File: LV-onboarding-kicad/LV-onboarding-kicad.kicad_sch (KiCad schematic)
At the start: 0 parts

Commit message: 2nd commit
changed the text in the bottom left of schematic
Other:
- title: ${BSPD_Circuit} -> BSPD_Circuit
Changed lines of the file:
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@@
 	(paper "A")
 	(title_block
-		(title "${BSPD_Circuit}")
+		(title "BSPD_Circuit")
 		(date "${CURRENT_DATE}")
 		(rev "${REVISION}")
 		(company "Formula Slug")
 		(comment 1 "Charles Ge")
-		(comment 3 "${COMMENT2}")
+		(comment 2 "Figured out how to push onto github after 4 hrs. I think in the future")
+		(comment 3 "it would be easier to hold github workshops with the desktop app")
+		(comment 4 "unless there is a benefit I am not aware of that is only in terminal.")
 	)
 	(sheet_instances

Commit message: commit1 friday
just put the haas sensor symbol on schematic
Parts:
- added U1: Current Transducer HASS 50 ... 600-S, Package_DFN_QFN:QFN-20-1EP_5x5mm_P0.65mm_EP3.35x3.35mm, symbol Connector:Conn_01x04_Pin
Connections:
- new net +5V: U1.4 (Pin_4)
- new net GND: U1.3 (Pin_3)
- new net OUTPUT: U1.2 (Pin_2)
- new net Vref: U1.1 (Pin_1)
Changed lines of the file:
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@@
 		(comment 4 "unless there is a benefit I am not aware of that is only in terminal.")
+	)
+	(label "GND"
+		(at 93.98 93.98 0)
+		(effects
+			(font
+				(size 1.27 1.27)
+			)
+			(justify left bottom)
+		)
+	)
+	(label "Vref"
+		(at 93.98 88.9 0)
+		(effects
+			(font
+				(size 1.27 1.27)
+			)
+			(justify left bottom)
+		)
+	)
+	(label "OUTPUT"
+		(at 93.98 91.44 0)
+		(effects
+			(font
+				(size 1.27 1.27)
+			)
+			(justify left bottom)
+		)
+	)
+	(label "+5V"
+		(at 93.98 96.52 0)
+		(effects
+			(font
+				(size 1.27 1.27)
+			)
+			(justify left bottom)
+		)
+	)
+	(symbol
+		(lib_id "Connector:Conn_01x04_Pin")
+		(at 88.9 91.44 0)
+		(unit 1)
+		(body_style 1)
+		(exclude_from_sim no)
+		(in_bom yes)
+		(on_board yes)
+		(in_pos_files yes)
+		(dnp no)
+		(fields_autoplaced yes)
+		(property "Reference" "U1"
+			(at 89.535 83.82 0)
+			(show_name no)
+			(do_not_autoplace no)
+			(effects
+				(font
+					(size 1.27 1.27)
+				)
+			)
+		)
+		(property "Value" "Current Transducer HASS 50 ... 600-S"
+			(at 89.535 86.36 0)
+			(show_name no)
+			(do_not_autoplace no)
+			(effects
+				(font
+					(size 1.27 1.27)
+				)
+			)
+		)
+		(property "Footprint" "Package_DFN_QFN:QFN-20-1EP_5x5mm_P0.65mm_EP3.35x3.35mm"
+			(at 88.9 91.44 0)
+			(hide yes)
+			(show_name no)
+			(do_not_autoplace no)
+			(effects
+				(font
+					(size 1.27 1.27)
+				)
+			)
+		)
+		(property "Datasheet" ""
+			(at 88.9 91.44 0)
+			(hide yes)
+			(show_name no)
+			(do_not_autoplace no)
+			(effects
+				(font
+					(size 1.27 1.27)
+				)
+			)
+		)
+		(property "Description" "Generic connector, single row, 01x04, script generated"
+			(at 88.9 91.44 0)
+			(hide yes)
+			(show_name no)
+			(do_not_autoplace no)
+			(effects
+				(font
+					(size 1.27 1.27)
+				)
+			)
+		)
+		(pin "3"
+		)
+		(pin "1"
+		)
+		(pin "4"
+		)
+		(pin "2"
+		)
+		(instances
+			(project "LV-onboarding-kicad"
+				(path "/e994741c-7c7d-4124-9d00-43b883baa61d"
+					(reference "U1")
+					(unit 1)
+				)
+			)
+		)
 	)
 	(sheet_instances

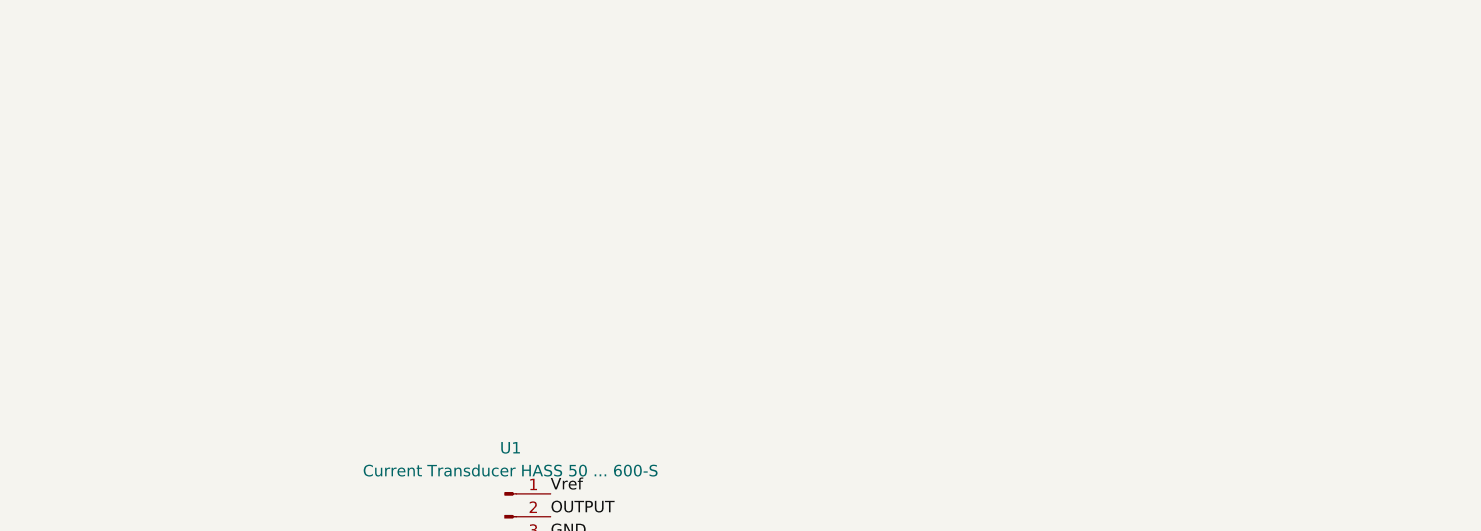
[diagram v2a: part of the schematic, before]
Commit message: kicad changes
put a couple more symbols into kicad schematic for BSPD
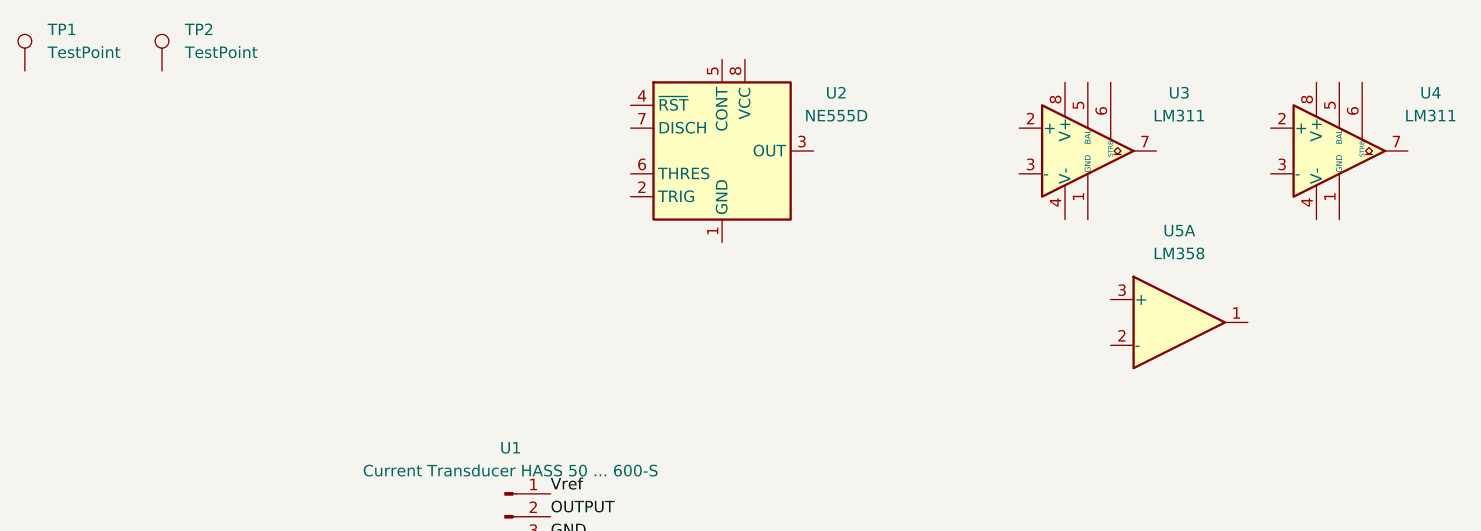
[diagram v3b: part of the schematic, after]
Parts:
- added TP1: TestPoint, Relay_THT:Relay_DPDT_Schrack-RT2-FormC_RM5mm, symbol Connector:TestPoint
- added TP2: TestPoint, symbol Connector:TestPoint
- added U2: NE555D, Package_SO:SOIC-8_3.9x4.9mm_P1.27mm, symbol Timer:NE555D
- added U3: LM311, Package_DIP:DIP-14_W7.62mm, symbol Comparator:LM311
- added U4: LM311, symbol Comparator:LM311
- added U5: LM358, Package_DFN_QFN:DFN-8-1EP_2x2mm_P0.5mm_EP1.05x1.75mm, symbol Amplifier_Operational:LM358

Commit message: ?
why it want me to commit again
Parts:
- removed U3: LM311, Package_DIP:DIP-14_W7.62mm, symbol Comparator:LM311
- removed U4: LM311, symbol Comparator:LM311
- removed U5: LM358, Package_DFN_QFN:DFN-8-1EP_2x2mm_P0.5mm_EP1.05x1.75mm, symbol Amplifier_Operational:LM358
- added J2: AiM Sports Pressure Sensors X05PSA02000P18, Package_DFN_QFN:QFN-20-1EP_5x5mm_P0.65mm_EP3.35x3.35mm, symbol Connector:Conn_01x03_Pin
- added U2, U3: ${SIM.PARAMS}, Package_SO:SSOP-24_3.9x8.7mm_P0.635mm, symbol Simulation_SPICE:OPAMP
- renumbered U1 to J1, U2 to U1
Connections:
- net GND: now also J2.2 (Pin_2)
- new net Analog Signal: J2.1 (Pin_1)
- new net Power Supply: J2.3 (Pin_3)

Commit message: kicad
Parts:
- added C1, C2: C, Package_SO:SOIC-8_3.9x4.9mm_P1.27mm, symbol Device:C
- added D1: D, symbol Device:D
- added K1: Relay_SPST-NO, Relay_THT:Relay_NCR_HHG1D-1, symbol Relay:Relay_SPST-NO
- added R1: R, Package_DIP:DIP-8_W7.62mm, symbol Device:R
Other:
- moved on the sheet: J1, J2, TP1, TP2, U1, U2, U3

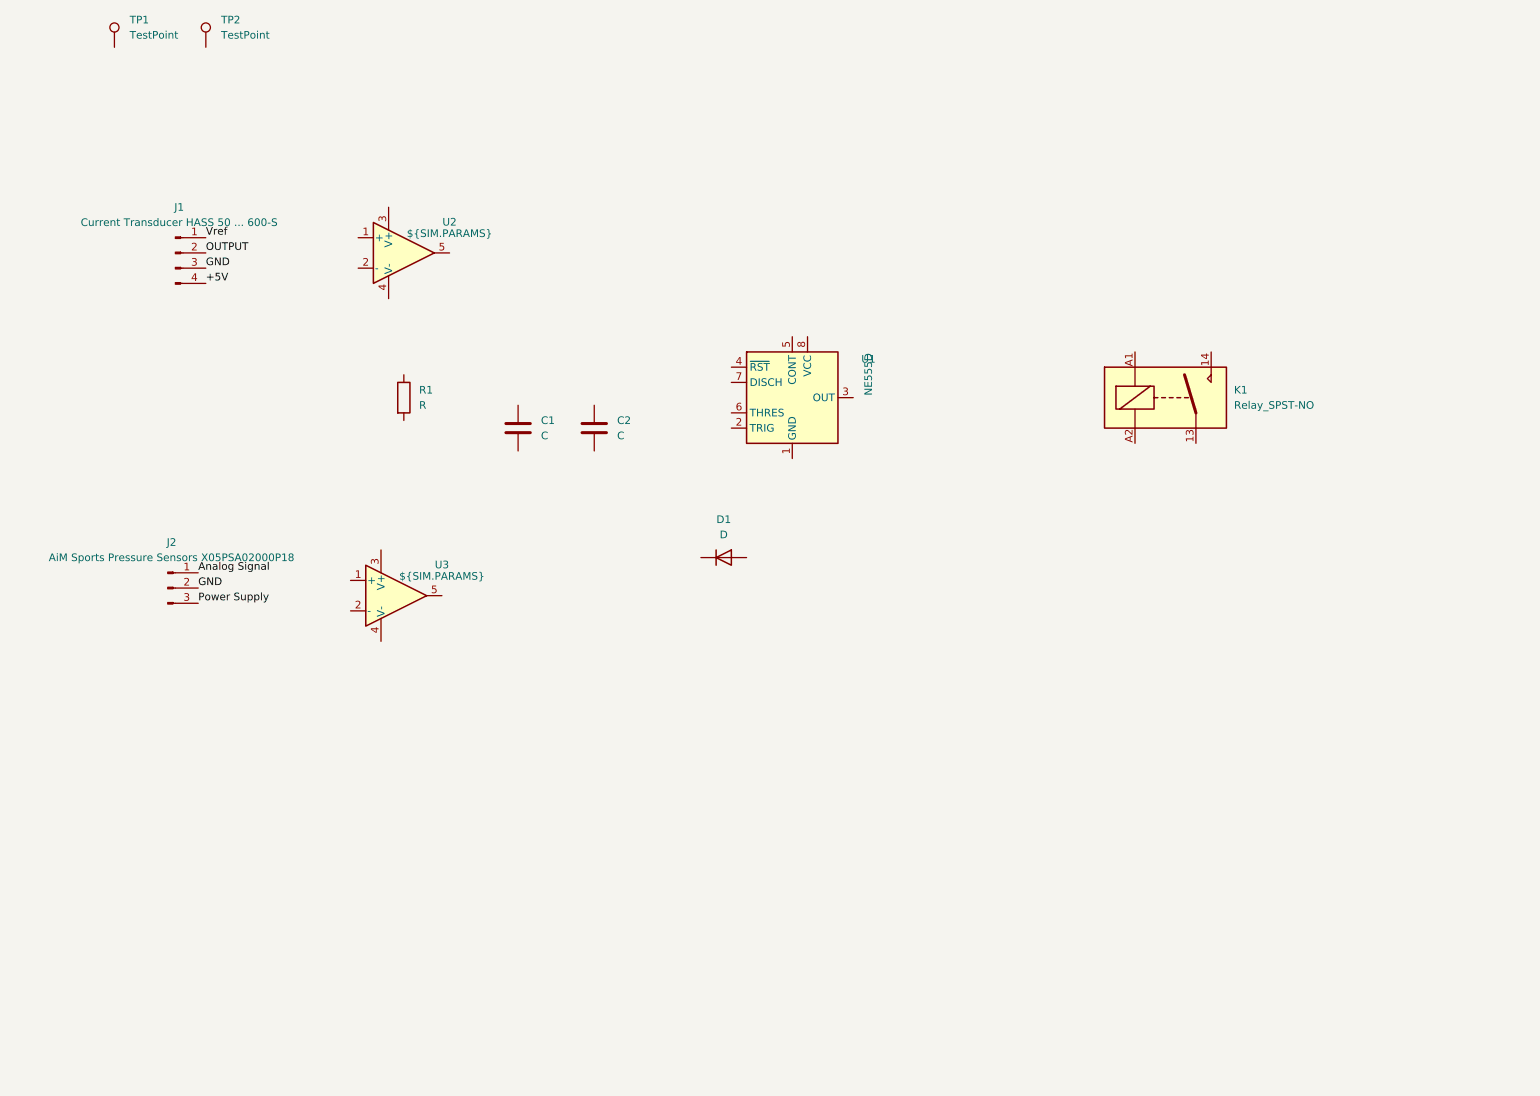
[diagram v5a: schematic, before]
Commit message: BSPD first comparator
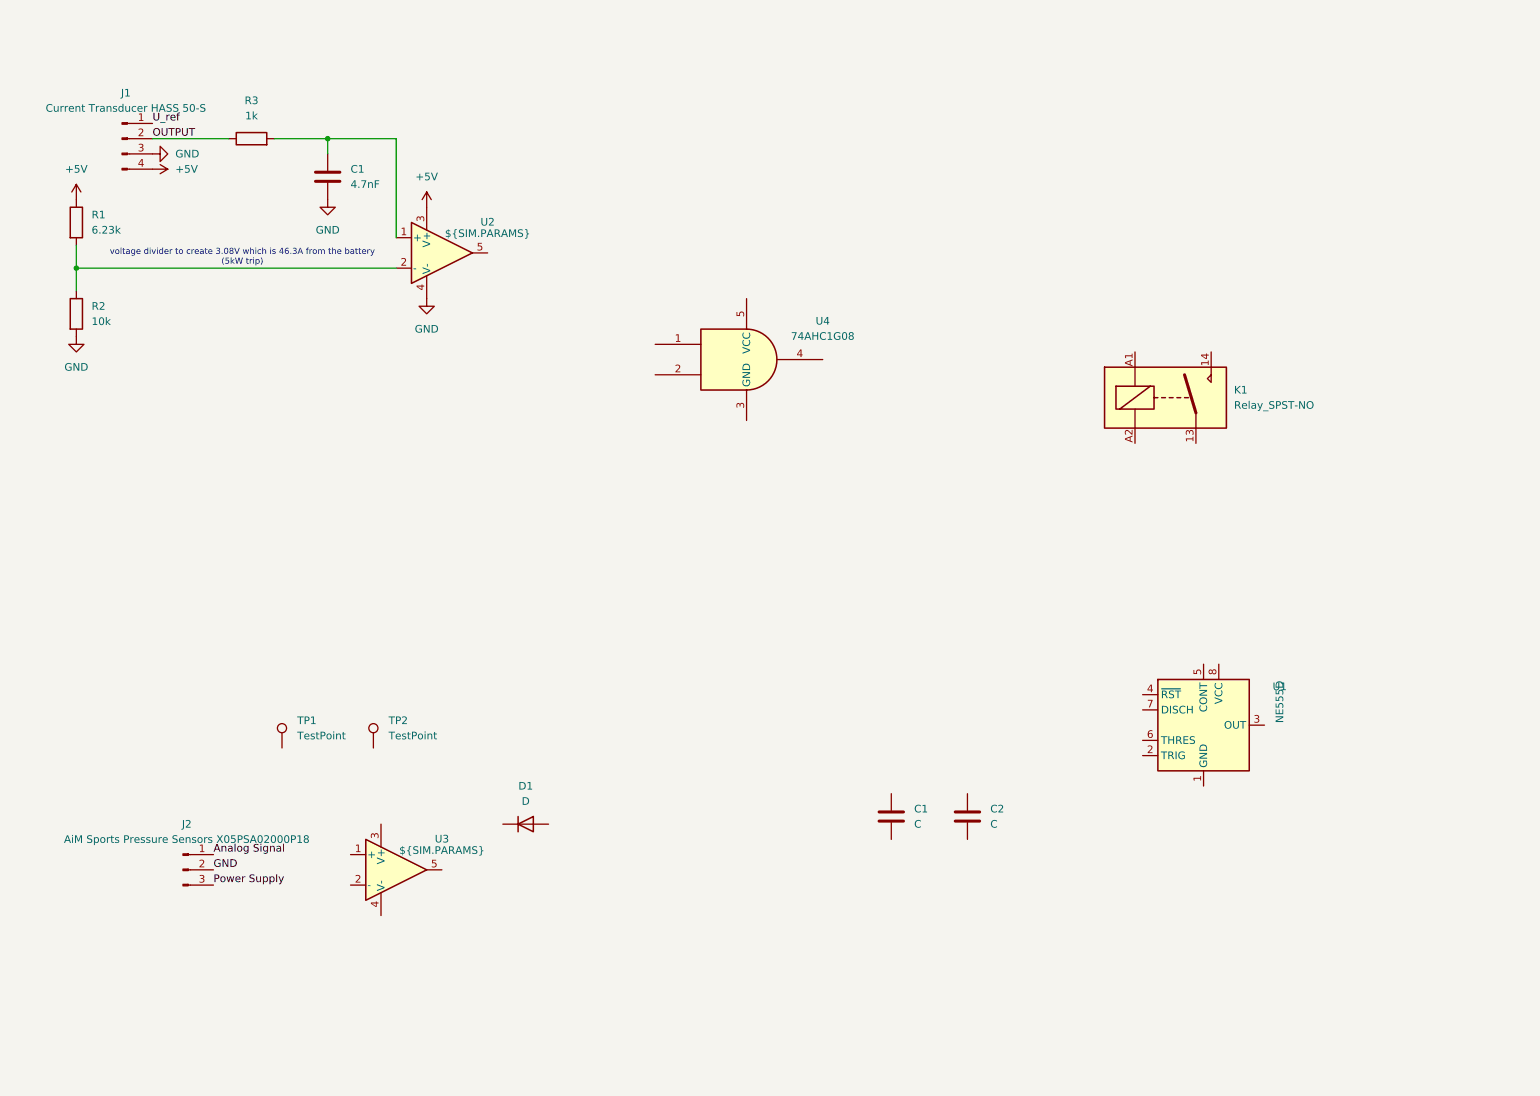
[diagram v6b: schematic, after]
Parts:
- added C1: 4.7nF, Package_SO:SOIC-8_3.9x4.9mm_P1.27mm, symbol Device:C
- added R1: 6.23k, symbol Device:R
- added R2: 10k, symbol Device:R
- added U4: 74AHC1G08, Package_SON:USON-20_2x4mm_P0.4mm, symbol 74xGxx:74AHC1G08
- J1: value Current Transducer HASS 50 ... 600-S -> Current Transducer HASS 50-S
- R3: renamed from R1; value R -> 1k
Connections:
- net +5V: now also U2.3 (V+), R1.1
- net GND: now also U2.4 (V-), C1.2, R2.2
- net OUTPUT: now also R3.1
- net at U2.1 (+): now also R3.2, C1.1
- net at U2.2 (-): now also R1.2, R2.1
- net Vref renamed U_ref
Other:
- note added: "voltage divider to create 3.08V which is 46.3A from the battery (5kW trip)"
- moved on the sheet: C1, C2, D1, J1, J2, R3, TP1, TP2, U1, U2, U3

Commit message: after Kicad workshop
learned about small version of symbols so I switched everything to its small version
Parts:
- removed C1: 4.7nF, Package_SO:SOIC-8_3.9x4.9mm_P1.27mm, symbol Device:C
- removed C1, C2: C, Package_SO:SOIC-8_3.9x4.9mm_P1.27mm, symbol Device:C
- removed D1: D, symbol Device:D
- removed R1: 6.23k, symbol Device:R
- removed R2: 10k, symbol Device:R
- removed R3: 1k, Package_DIP:DIP-8_W7.62mm, symbol Device:R
- removed TP1: TestPoint, Relay_THT:Relay_DPDT_Schrack-RT2-FormC_RM5mm, symbol Connector:TestPoint
- removed TP2: TestPoint, symbol Connector:TestPoint
- added C1: 4.7nF, Package_SO:SOIC-8_3.9x4.9mm_P1.27mm, symbol Device:C_Small
- added R1: 6.23k, symbol Device:R_Small
- added R2: 10k, symbol Device:R_Small
- added R3: 1k, symbol Device:R_Small
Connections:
- net +5V: now also R1.1
- net GND: now also C1.2, R2.2
- net OUTPUT: now also R3.1
- net at U2.1 (+): now also C1.1, R3.2
- net at U2.2 (-): now also R1.2, R2.1

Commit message: brake sensor op amps
finished brake sensor op amp pressure level and the short testing. will need to find voltage values later
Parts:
- removed J2: AiM Sports Pressure Sensors X05PSA02000P18, Package_DFN_QFN:QFN-20-1EP_5x5mm_P0.65mm_EP3.35x3.35mm, symbol Connector:Conn_01x03_Pin
- added C2: 4.7nF, symbol Device:C_Small
- added J2: AiM Sports Pressure Sensors X05PSA02000P18, Package_DFN_QFN:QFN-20-1EP_5x5mm_P0.65mm_EP3.35x3.35mm, symbol Connector_Generic:Conn_01x03
- added R4: FIND VALUE NEEEDED FOR THIS, symbol Device:R_Small
- added R5, R7, R9: FIND VALUE NEEDED, symbol Device:R_Small
- added R6, R8: FIND VALUE NEEEDED, symbol Device:R_Small
- added U1b, U1c: ${SIM.PARAMS}, Package_TO_SOT_SMD:SOT-353_SC-70-5, symbol Simulation_SPICE:OPAMP
- renumbered U3 to U1a
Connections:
- net +5V: now also U1.8 (VCC), U1a.3 (V+), U4.5 (VCC), R4.1, R6.1, R8.1, U1b.3 (V+), U1c.3 (V+)
- net Analog Signal: now also U1a.1 (+), C2.1, J2.1 (Pin_1), U1b.1 (+), U1c.2 (-)
- net GND: now also U1.1 (GND), U1a.4 (V-), U4.3 (GND), C2.2, J2.2 (Pin_2), R5.2, R7.2, R9.2, U1b.4 (V-), U1c.4 (V-)
- net Power Supply: now also J2.3 (Pin_3)
- net BRAKE_HIGH_OK: now reaches U4.1
- net BRAKE_HIGH_OK: now also U1c.5
- net BRAKE_LOW_OK: now reaches U4.2
- net BRAKE_LOW_OK: now also U1b.5
- net BRAKE_OK: now reaches U4.4
- net at U1a.2 (-): now also R4.2, R5.1
- net BRAKE_HIGH: now reaches U1a.5
- new net: R6.2, R7.1, U1b.2 (-)
- new net: R8.2, R9.1, U1c.1 (+)
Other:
- note added: "capacitor for noise filter"
- moved on the sheet: K1, U1, U1a, U4
